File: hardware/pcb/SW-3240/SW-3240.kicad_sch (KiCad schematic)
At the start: 1 part, among them J1 OLED

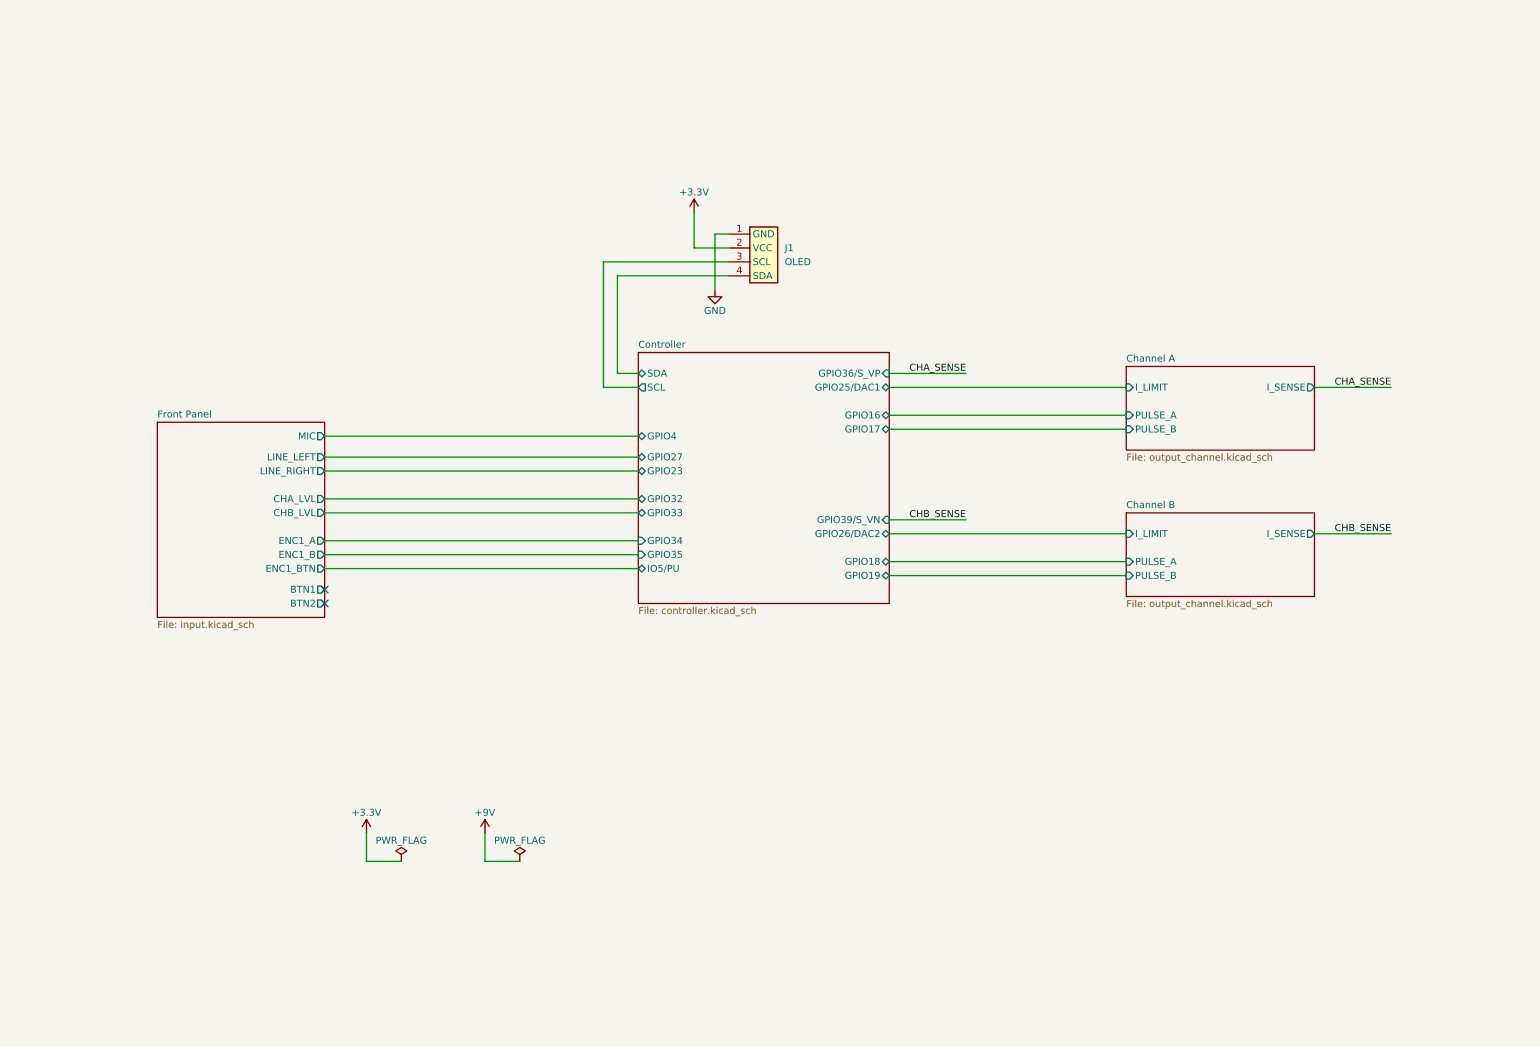
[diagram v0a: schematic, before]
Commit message: make SW-3240 modular
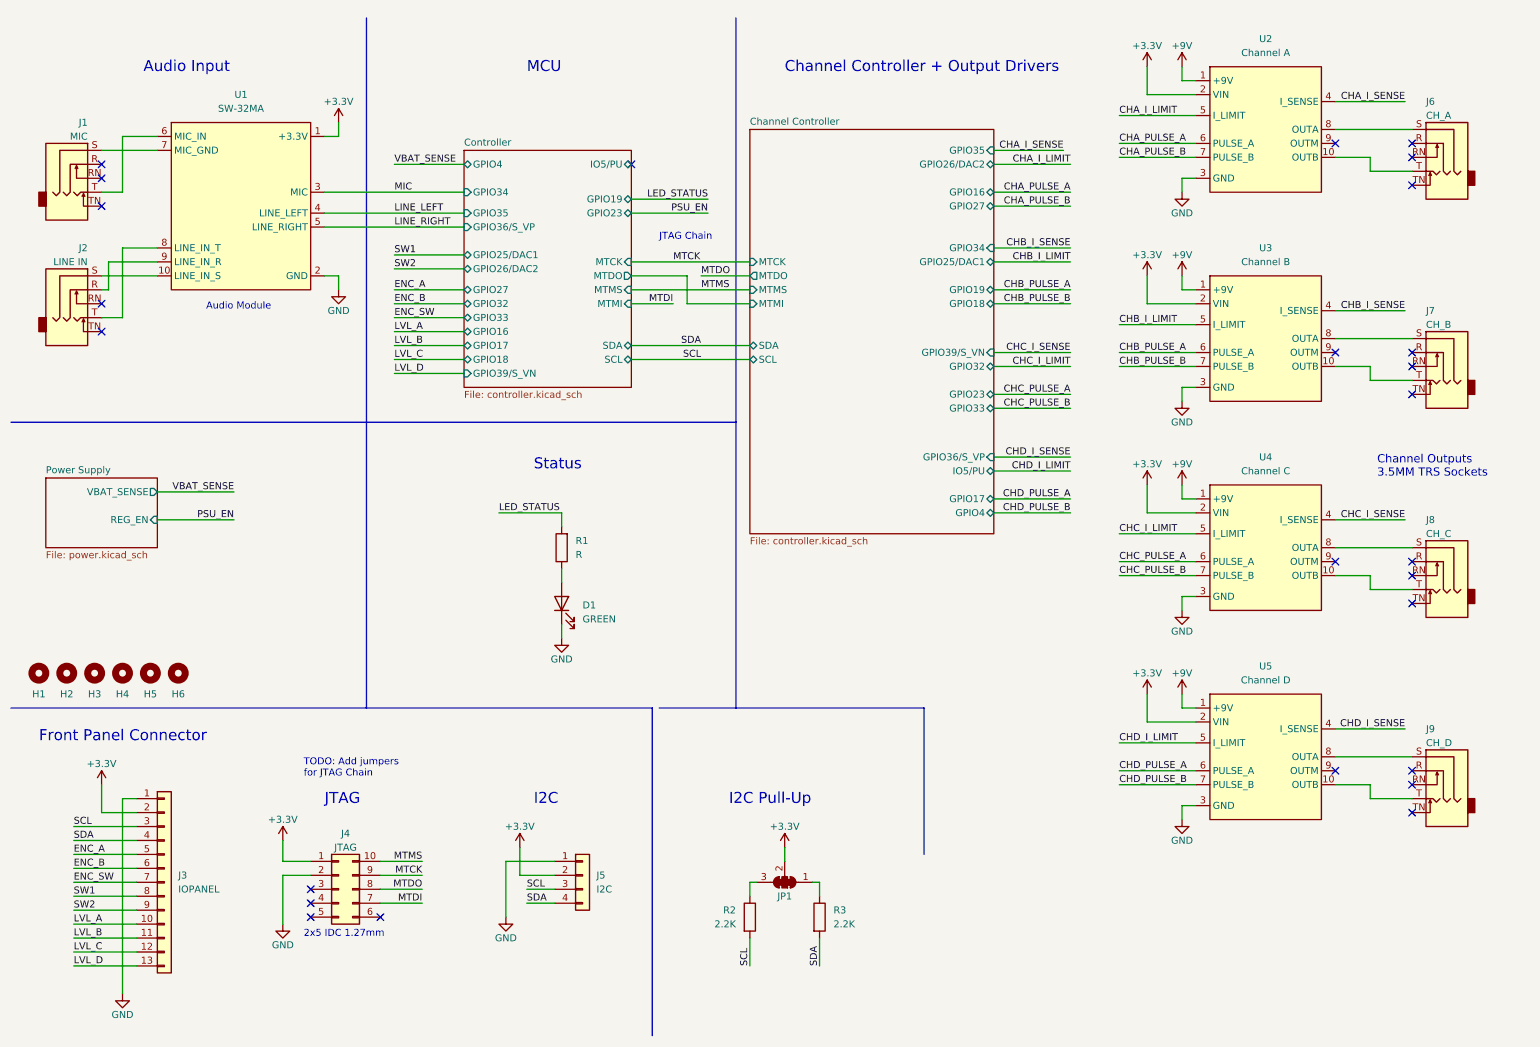
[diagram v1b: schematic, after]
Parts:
- removed J1: OLED, SaawLib:OLED_I2C, symbol SaawLib:OLED_MODULE_I2C
- added D1: GREEN, LED_SMD:LED_0805_2012Metric, symbol Device:LED
- added H1, H2, H3, H4, H5, H6: MountingHole, MountingHole:MountingHole_2.2mm_M2, symbol Mechanical:MountingHole
- added J1: MIC, SaawLib:STX-3100-5N, symbol Connector:AudioJack3_SwitchTR
- added J2: LINE IN, SaawLib:STX-3100-5N, symbol Connector:AudioJack3_SwitchTR
- added J3: IOPANEL, Connector_JST:JST_XH_B13B-XH-A_1x13_P2.50mm_Vertical, symbol Connector_Generic:Conn_01x13
- added J4: JTAG, Connector_PinHeader_1.27mm:PinHeader_2x05_P1.27mm_Vertical, symbol Connector_Generic:Conn_02x05_Counter_Clockwise
- added J5: I2C, Connector_PinHeader_2.54mm:PinHeader_1x04_P2.54mm_Vertical, symbol Connector_Generic:Conn_01x04
- added J6: CH_A, SaawLib:STX-3100-5N, symbol Connector:AudioJack3_SwitchTR
- added J7: CH_B, SaawLib:STX-3100-5N, symbol Connector:AudioJack3_SwitchTR
- added J8: CH_C, SaawLib:STX-3100-5N, symbol Connector:AudioJack3_SwitchTR
- added J9: CH_D, SaawLib:STX-3100-5N, symbol Connector:AudioJack3_SwitchTR
- added JP1: SolderJumper_3_Bridged123, SaawLib:SolderJumper-3_P1.3mm_Bridged123_Pad1.0x1.5mm_NumberLabels, symbol Jumper:SolderJumper_3_Bridged123
- added R1: R, Resistor_SMD:R_0603_1608Metric, symbol Device:R
- added R2, R3: 2.2K, Resistor_SMD:R_0603_1608Metric, symbol Device:R
- added U1: SW-32MA, SaawLib:SW-32MA_Socket, symbol SaawLib:SW-32MA
- added U2: Channel A, SaawLib:SW-32MO_Socket, symbol SaawLib:SW-32MO
- added U3: Channel B, SaawLib:SW-32MO_Socket, symbol SaawLib:SW-32MO
- added U4: Channel C, SaawLib:SW-32MO_Socket, symbol SaawLib:SW-32MO
- added U5: Channel D, SaawLib:SW-32MO_Socket, symbol SaawLib:SW-32MO
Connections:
- net +3V3: now also J3.2 (Pin_2), J4.1 (Pin_1), J5.2 (Pin_2), JP1.2 (C), U1.1 (+3.3V), U2.2 (VIN), U3.2 (VIN), U4.2 (VIN), U5.2 (VIN)
- net +9V: now also U2.1 (+9V), U3.1 (+9V), U4.1 (+9V), U5.1 (+9V)
- net GND: now also D1.1 (K), J3.1 (Pin_1), J4.2 (Pin_2), J5.1 (Pin_1), U1.2 (GND), U2.3 (GND), U3.3 (GND), U4.3 (GND), U5.3 (GND)
- new net: J9.T, U5.10 (OUTB)
- new net: J9.S, U5.8 (OUTA)
- new net: D1.2 (A), R1.1
- new net: J6.S, U2.8 (OUTA)
- new net: J6.T, U2.10 (OUTB)
- new net: J7.S, U3.8 (OUTA)
- new net: J7.T, U3.10 (OUTB)
- new net: J1.S, U1.7 (MIC_GND)
- new net: J1.T, U1.6 (MIC_IN)
- new net: JP1.3 (B), R2.1
- new net: J8.S, U4.8 (OUTA)
- new net: J8.T, U4.10 (OUTB)
- new net: JP1.1 (A), R3.1
- new net: J2.S, U1.10 (LINE_IN_S)
- new net: J2.T, U1.8 (LINE_IN_T)
- new net: J2.R, U1.9 (LINE_IN_R)
- new net CHA_I_LIMIT: U2.5 (I_LIMIT)
- new net CHA_I_SENSE: U2.4 (I_SENSE)
- new net CHA_PULSE_A: U2.6 (PULSE_A)
- new net CHA_PULSE_B: U2.7 (PULSE_B)
- new net CHB_I_LIMIT: U3.5 (I_LIMIT)
- new net CHB_I_SENSE: U3.4 (I_SENSE)
- new net CHB_PULSE_A: U3.6 (PULSE_A)
- new net CHB_PULSE_B: U3.7 (PULSE_B)
- new net CHC_I_LIMIT: U4.5 (I_LIMIT)
- new net CHC_I_SENSE: U4.4 (I_SENSE)
- new net CHC_PULSE_A: U4.6 (PULSE_A)
- new net CHC_PULSE_B: U4.7 (PULSE_B)
- new net CHD_I_LIMIT: U5.5 (I_LIMIT)
- new net CHD_I_SENSE: U5.4 (I_SENSE)
- new net CHD_PULSE_A: U5.6 (PULSE_A)
- new net CHD_PULSE_B: U5.7 (PULSE_B)
- new net ENC_A: J3.5 (Pin_5)
- new net ENC_B: J3.6 (Pin_6)
- new net ENC_SW: J3.7 (Pin_7)
- new net LED_STATUS: R1.2
- new net LINE_LEFT: U1.4 (LINE_LEFT)
- new net LINE_RIGHT: U1.5 (LINE_RIGHT)
- new net LVL_A: J3.10 (Pin_10)
- new net LVL_B: J3.11 (Pin_11)
- new net LVL_C: J3.12 (Pin_12)
- new net LVL_D: J3.13 (Pin_13)
- new net MIC: U1.3 (MIC)
- new net MTCK: J4.9 (Pin_9)
- new net MTDI: J4.7 (Pin_7)
- new net MTDO: J4.8 (Pin_8)
- new net MTMS: J4.10 (Pin_10)
- new net SCL: J3.3 (Pin_3), J5.3 (Pin_3), R2.2
- new net SDA: J3.4 (Pin_4), J5.4 (Pin_4), R3.2
- new net SW1: J3.8 (Pin_8)
- new net SW2: J3.9 (Pin_9)
- no-connect marks 2 -> 26
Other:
- removed sheet Channel A
- removed sheet Channel B
- removed sheet Front Panel
- added sheet Channel Controller (controller.kicad_sch)
- added sheet Power Supply (power.kicad_sch)
- sheet Controller ports: added MTCK, MTDO, MTMI, MTMS; removed none
- note added: "2x5 IDC 1.27mm"
- note added: "Audio Input"
- note added: "Audio Module"
- note added: "Channel Controller + Output Drivers"
- note added: "Channel Outputs 3.5MM TRS Sockets"
- note added: "Front Panel Connector"
- note added: "I2C"
- note added: "I2C Pull-Up"
- note added: "JTAG"
- note added: "JTAG Chain"
- note added: "MCU"
- note added: "Status"
- note added: "TODO: Add jumpers for JTAG Chain"
- title: SW-3221 -> SW-3240

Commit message: split dual esp32 modules
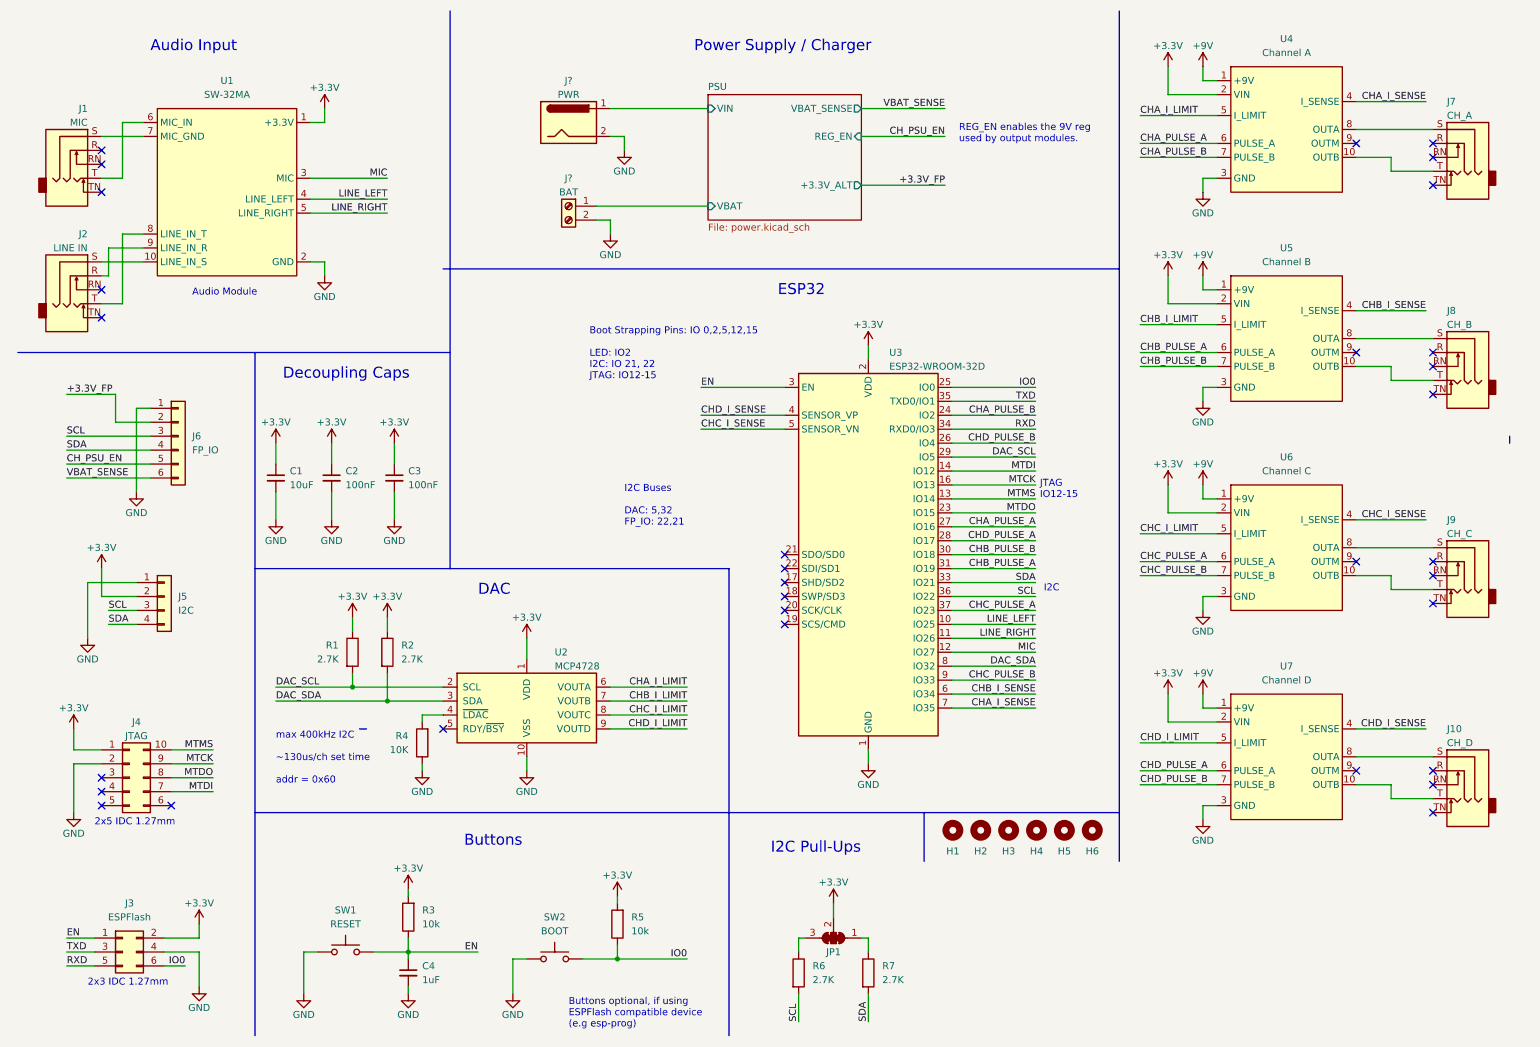
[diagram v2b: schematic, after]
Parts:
- removed D1: GREEN, LED_SMD:LED_0805_2012Metric, symbol Device:LED
- removed J3: IOPANEL, Connector_JST:JST_XH_B13B-XH-A_1x13_P2.50mm_Vertical, symbol Connector_Generic:Conn_01x13
- removed J6: CH_A, SaawLib:STX-3100-5N, symbol Connector:AudioJack3_SwitchTR
- removed U2: Channel A, SaawLib:SW-32MO_Socket, symbol SaawLib:SW-32MO
- removed U3: Channel B, SaawLib:SW-32MO_Socket, symbol SaawLib:SW-32MO
- added C1: 10uF, Capacitor_SMD:C_0603_1608Metric, symbol Device:C_Small
- added C2, C3: 100nF, Capacitor_SMD:C_0603_1608Metric, symbol Device:C_Small
- added C4: 1uF, Capacitor_SMD:C_0603_1608Metric, symbol Device:C_Small
- added J10: CH_D, SaawLib:STX-3100-5N, symbol Connector:AudioJack3_SwitchTR
- added J3: ESPFlash, Connector_PinHeader_1.27mm:PinHeader_2x03_P1.27mm_Vertical, symbol Connector_Generic:Conn_02x03_Odd_Even
- added J6: FP_IO, symbol Connector_Generic:Conn_01x06
- added J?: PWR, SaawLib:BarrelJack_CUI_PJ-102AH_Horizontal, symbol Connector:Barrel_Jack
- added J?: BAT, Connector_JST:JST_XH_B2B-XH-A_1x02_P2.50mm_Vertical, symbol Connector:Screw_Terminal_01x02
- added R4: 10K, Resistor_SMD:R_0603_1608Metric, symbol Device:R
- added R5: 10k, Resistor_SMD:R_0603_1608Metric, symbol Device:R
- added R6, R7: 2.7K, Resistor_SMD:R_0603_1608Metric, symbol Device:R
- added SW1: RESET, Button_Switch_SMD:SW_Push_SPST_NO_Alps_SKRK, symbol Switch:SW_Push
- added SW2: BOOT, Button_Switch_SMD:SW_Push_SPST_NO_Alps_SKRK, symbol Switch:SW_Push
- added U2: MCP4728, Package_SO:MSOP-10_3x3mm_P0.5mm, symbol Analog_DAC:MCP4728
- added U3: ESP32-WROOM-32D, RF_Module:ESP32-WROOM-32, symbol RF_Module:ESP32-WROOM-32D
- added U6: Channel C, SaawLib:SW-32MO_Socket, symbol SaawLib:SW-32MO
- added U7: Channel D, SaawLib:SW-32MO_Socket, symbol SaawLib:SW-32MO
- J7: value CH_B -> CH_A
- J8: value CH_C -> CH_B
- J9: value CH_D -> CH_C
- R1: value R -> 2.7K
- R2: value 2.2K -> 2.7K
- R3: value 2.2K -> 10k
- U4: value Channel C -> Channel A
- U5: value Channel D -> Channel B
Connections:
- net +3V3: now also R1.1, R2.1, R3.2, C1.1, C2.1, C3.1, J3.2 (Pin_2), R5.2, U2.1 (VDD), U3.2 (VDD), U6.2 (VIN), U7.2 (VIN)
- net +9V: now also U6.1 (+9V), U7.1 (+9V)
- net CHA_I_LIMIT: now also U4.5 (I_LIMIT), U2.6 (VOUTA)
- net CHA_I_SENSE: now also U4.4 (I_SENSE), U3.7 (IO35)
- net CHA_PULSE_A: now also U4.6 (PULSE_A), U3.27 (IO16)
- net CHA_PULSE_B: now also U4.7 (PULSE_B), U3.24 (IO2)
- net CHB_I_LIMIT: now also U5.5 (I_LIMIT), U2.7 (VOUTB)
- net CHB_I_SENSE: now also U5.4 (I_SENSE), U3.6 (IO34)
- net CHB_PULSE_A: now also U5.6 (PULSE_A), U3.31 (IO19)
- net CHB_PULSE_B: now also U5.7 (PULSE_B), U3.30 (IO18)
- net CHC_I_LIMIT: now also U2.8 (VOUTC), U6.5 (I_LIMIT); no longer U4.5 (I_LIMIT)
- net CHC_I_SENSE: now also U3.5 (SENSOR_VN), U6.4 (I_SENSE); no longer U4.4 (I_SENSE)
- net CHC_PULSE_A: now also U3.37 (IO23), U6.6 (PULSE_A); no longer U4.6 (PULSE_A)
- net CHC_PULSE_B: now also U3.9 (IO33), U6.7 (PULSE_B); no longer U4.7 (PULSE_B)
- net CHD_I_LIMIT: now also U2.9 (VOUTD), U7.5 (I_LIMIT); no longer U5.5 (I_LIMIT)
- net CHD_I_SENSE: now also U3.4 (SENSOR_VP), U7.4 (I_SENSE); no longer U5.4 (I_SENSE)
- net CHD_PULSE_A: now also U3.28 (IO17), U7.6 (PULSE_A); no longer U5.6 (PULSE_A)
- net CHD_PULSE_B: now also U3.26 (IO4), U7.7 (PULSE_B); no longer U5.7 (PULSE_B)
- net GND: now also C1.2, C2.2, C3.2, C4.2, J3.4 (Pin_4), J6.1 (Pin_1), J?.2, J?.2 (Pin_2), R4.1, SW1.1, SW2.1, U2.10 (VSS), U3.1 (GND), U3.15 (GND), U3.38 (GND), U3.39 (GND), U6.3 (GND), U7.3 (GND)
- net LINE_LEFT: now also U3.10 (IO25)
- net LINE_RIGHT: now also U3.11 (IO26)
- net MIC: now also U3.12 (IO27)
- net MTCK: now also U3.16 (IO13)
- net MTDI: now also U3.14 (IO12)
- net MTDO: now also U3.23 (IO15)
- net MTMS: now also U3.13 (IO14)
- net SCL: now also J6.3 (Pin_3), R6.2, U3.36 (IO22); no longer R2.2
- net SDA: now also J6.4 (Pin_4), R7.2, U3.33 (IO21); no longer R3.2
- net VBAT_SENSE: now also J6.6 (Pin_6)
- net at U5.10 (OUTB): now also J8.T; no longer J9.T
- net at U5.8 (OUTA): now also J8.S; no longer J9.S
- net at J7.S: now also U4.8 (OUTA)
- net at J7.T: now also U4.10 (OUTB)
- net at JP1.3 (B): now also R6.1; no longer R2.1
- net at JP1.1 (A): now also R7.1; no longer R3.1
- net LED_STATUS renamed DAC_SCL
- net DAC_SCL: now also U2.2 (SCL), U3.29 (IO5)
- new net: R4.2, U2.4 (~{LDAC})
- new net: J9.S, U6.8 (OUTA)
- new net: J9.T, U6.10 (OUTB)
- new net: J10.T, U7.10 (OUTB)
- new net: J10.S, U7.8 (OUTA)
- new net +3.3V_FP: J6.2 (Pin_2)
- new net CH_PSU_EN: J6.5 (Pin_5)
- new net DAC_SDA: R2.2, U2.3 (SDA), U3.8 (IO32)
- new net EN: C4.1, J3.1 (Pin_1), R3.1, SW1.2, U3.3 (EN)
- new net IO0: J3.6 (Pin_6), R5.1, SW2.2, U3.25 (IO0)
- new net PSU/VBAT: J?.1 (Pin_1)
- new net PSU/VIN: J?.1
- new net RXD: J3.5 (Pin_5), U3.34 (RXD0/IO3)
- new net TXD: J3.3 (Pin_3), U3.35 (TXD0/IO1)
- no-connect marks 26 -> 32
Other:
- removed sheet Channel Controller
- removed sheet Controller
- removed sheet Power Supply
- added sheet PSU (power.kicad_sch)
- note added: "2x3 IDC 1.27mm"
- note added: "Boot Strapping Pins: IO 0,2,5,12,15 LED: IO2 I2C: IO 21, 22 JTAG: IO12-15"
- note added: "Buttons"
- note added: "Buttons optional, if using ESPFlash compatible device (e.g esp-prog)"
- note added: "DAC"
- note added: "Decoupling Caps"
- note added: "ESP32"
- note added: "I2C Buses DAC: 5,32 FP_IO: 22,21"
- note added: "I2C Pull-Ups"
- note added: "JTAG IO12-15"
- note added: "Power Supply / Charger"
- note added: "REG_EN enables the 9V reg used by output modules."
- note added: "max 400kHz I2C ~130us/ch set time addr = 0x60"
- note removed: "Channel Controller + Output Drivers"
- note removed: "Channel Outputs 3.5MM TRS Sockets"
- note removed: "Front Panel Connector"
- note removed: "I2C Pull-Up"
- note removed: "JTAG"
- note removed: "JTAG Chain"
- note removed: "MCU"
- note removed: "Status"
- note removed: "TODO: Add jumpers for JTAG Chain"
- company: (none) -> saawsm
